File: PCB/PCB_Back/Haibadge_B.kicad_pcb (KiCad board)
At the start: 2 copper layers, 79.8 x 79.8 mm, 77 parts, among them J1 Sensor connector, J2 USB_C_Receptacle_USB2.0, J3 Lipo connector, Q1 UMH3N, Q3 Q_PMOS_GSD, SW1 SW_Push_Dual, SW2 SW_PWR, U1 ESP-12E, U2 CH340C, U3 MCP73831-2-OT, U4 MCP1700x-330xxTT, U6 BME680

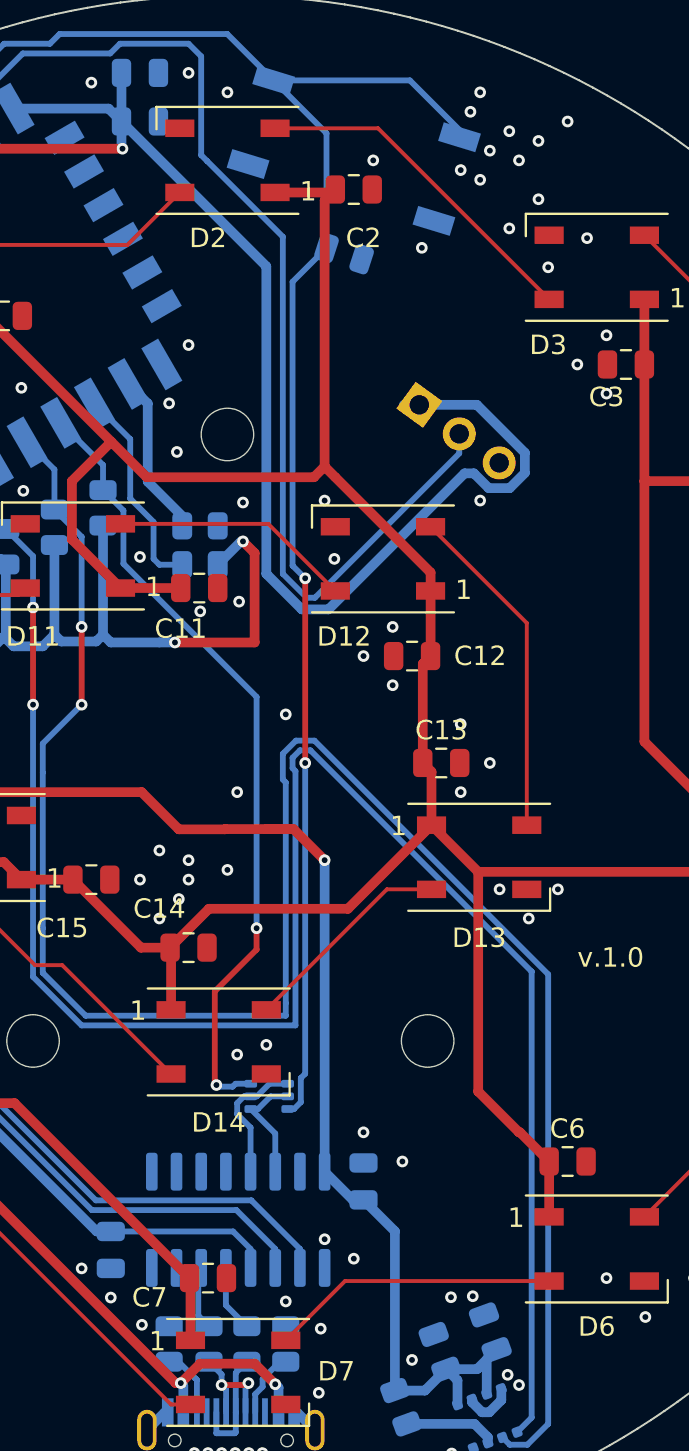
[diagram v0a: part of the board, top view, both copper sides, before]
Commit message: Change J1 to SMD, Production
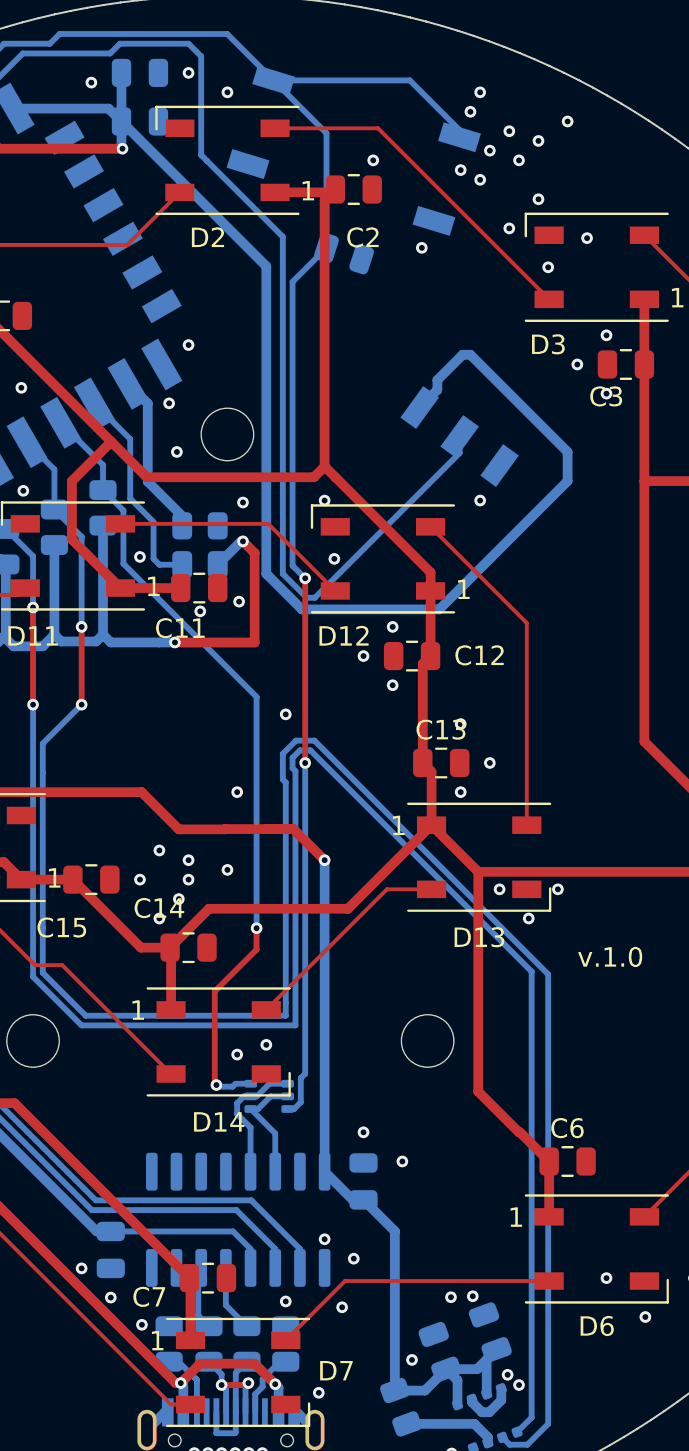
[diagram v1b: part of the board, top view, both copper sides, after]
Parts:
- J1: footprint Connector_PinSocket_2.54mm:PinSocket_1x03_P2.54mm_Horizontal -> easyeda2kicad:HDR-SMD_3P-P2.54-H-F-L11.5
- moved J1 2.64 mm to (151.9, 122.7), turned to -36 degrees
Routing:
- net +3V3: track 257.7 -> 263.4 mm

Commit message: Fixed Typo, added new ibom
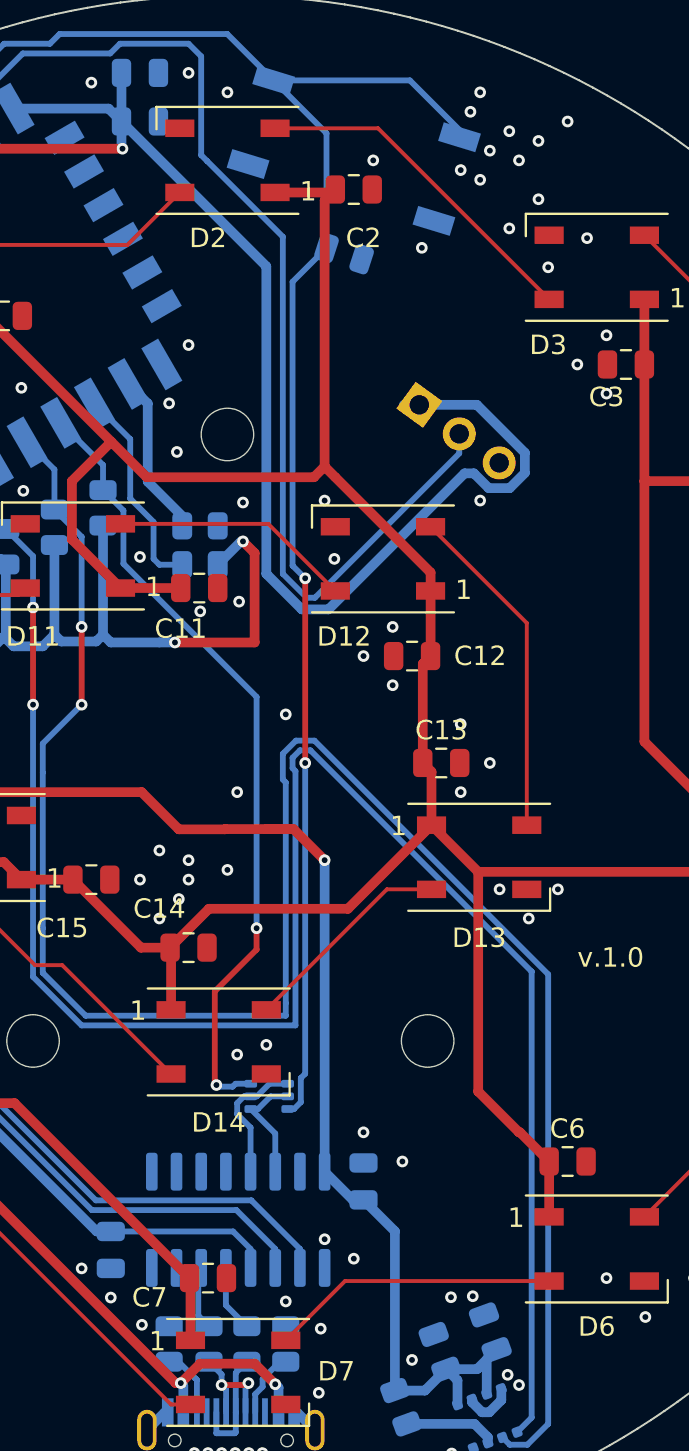
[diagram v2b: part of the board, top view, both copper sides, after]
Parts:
- J1: footprint easyeda2kicad:HDR-SMD_3P-P2.54-H-F-L11.5 -> Connector_PinSocket_2.54mm:PinSocket_1x03_P2.54mm_Horizontal
- R4: value 2k -> 1k
- moved J1 2.64 mm to (149.9, 121.1), turned to -126 degrees
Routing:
- net +3V3: track 263.4 -> 257.7 mm
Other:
- board text added: "Blahaj Pentagramm Badge v2.0 (2024) Waldo und vielleicht Peter"
- board text removed: "Blahaj Pentgramm Badge v2.0 (2024) Waldo und vielleicht Peter"

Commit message: Revert "Fixed Typo, added new ibom"
This reverts commit 21eb23da6b9f4b1b78e37bb966b9e164ecd6150b.
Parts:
- J1: footprint Connector_PinSocket_2.54mm:PinSocket_1x03_P2.54mm_Horizontal -> easyeda2kicad:HDR-SMD_3P-P2.54-H-F-L11.5
- R4: value 1k -> 2k
- moved J1 2.64 mm to (151.9, 122.7), turned to -36 degrees
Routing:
- net +3V3: track 257.7 -> 263.4 mm
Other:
- board text added: "Blahaj Pentgramm Badge v2.0 (2024) Waldo und vielleicht Peter"
- board text removed: "Blahaj Pentagramm Badge v2.0 (2024) Waldo und vielleicht Peter"

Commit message: Fixed Typo, added new ibom
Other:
- board text added: "Blahaj Pentagramm Badge v2.0 (2024) Waldo und vielleicht Peter"
- board text removed: "Blahaj Pentgramm Badge v2.0 (2024) Waldo und vielleicht Peter"
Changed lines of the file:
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@@
 		)
 	)
-	(gr_text "Blahaj Pentgramm Badge\nv2.0 (2024)\nWaldo\nund\nvielleicht Peter"
-		(at 166 157.5 -90)
+	(gr_text "Blahaj Pentagramm Badge\nv2.0 (2024)\nWaldo\nund\nvielleicht Peter"
+		(at 166 157.5 270)
 		(layer "B.SilkS")
 		(effects
